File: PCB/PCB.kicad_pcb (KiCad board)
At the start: 2 copper layers, 100 x 89.4 mm, 34 parts, among them SW1 SW_Push, SW10 RotaryEncoder_Switch, SW2 SW_Push, SW3 SW_Push, SW4 SW_Push, SW5 SW_Push, SW6 SW_Push, SW7 SW_Push, SW8 SW_Push, SW9 SW_Push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

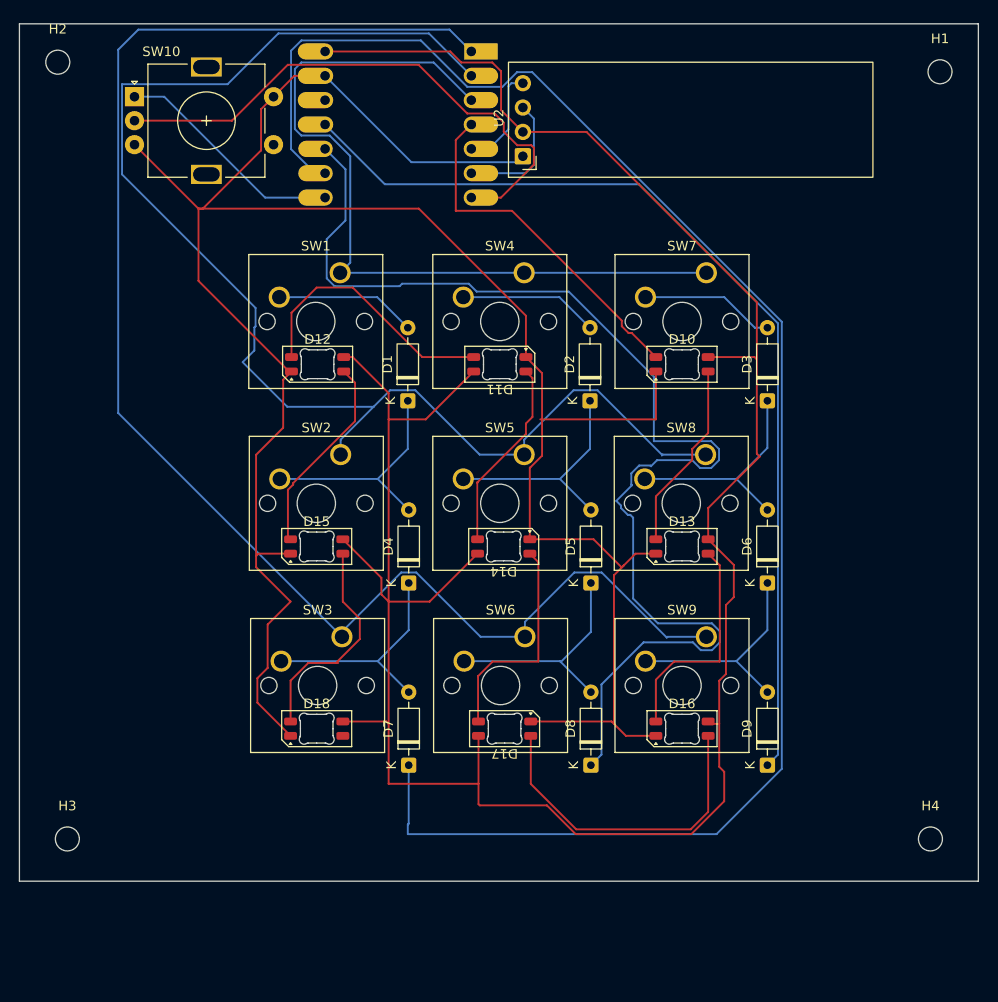
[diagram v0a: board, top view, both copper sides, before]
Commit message: Created PCB and CAD for casing
Also slightly changed positioning and size of PCB
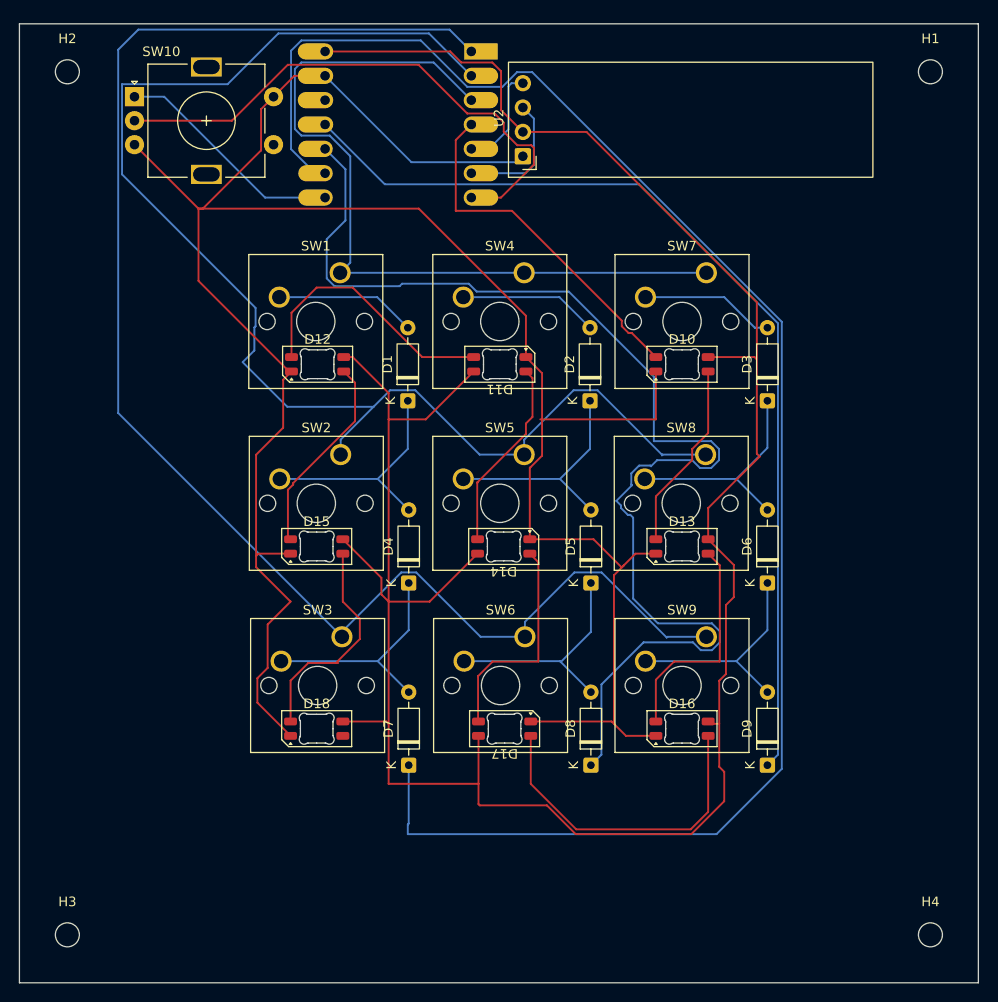
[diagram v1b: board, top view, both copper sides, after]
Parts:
- moved H3 10.0 mm to (65.0, 117.5)
- moved H4 10.0 mm to (155.0, 117.5)
- moved H2 1.41 mm to (65.0, 27.5)
- moved H1 1.00 mm to (155.0, 27.5)
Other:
- board size 100 x 89.4 mm -> 100 x 100 mm
